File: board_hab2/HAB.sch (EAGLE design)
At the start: 39 parts, among them Q1 2N5496, Q2 2N5496, T2 2N3904

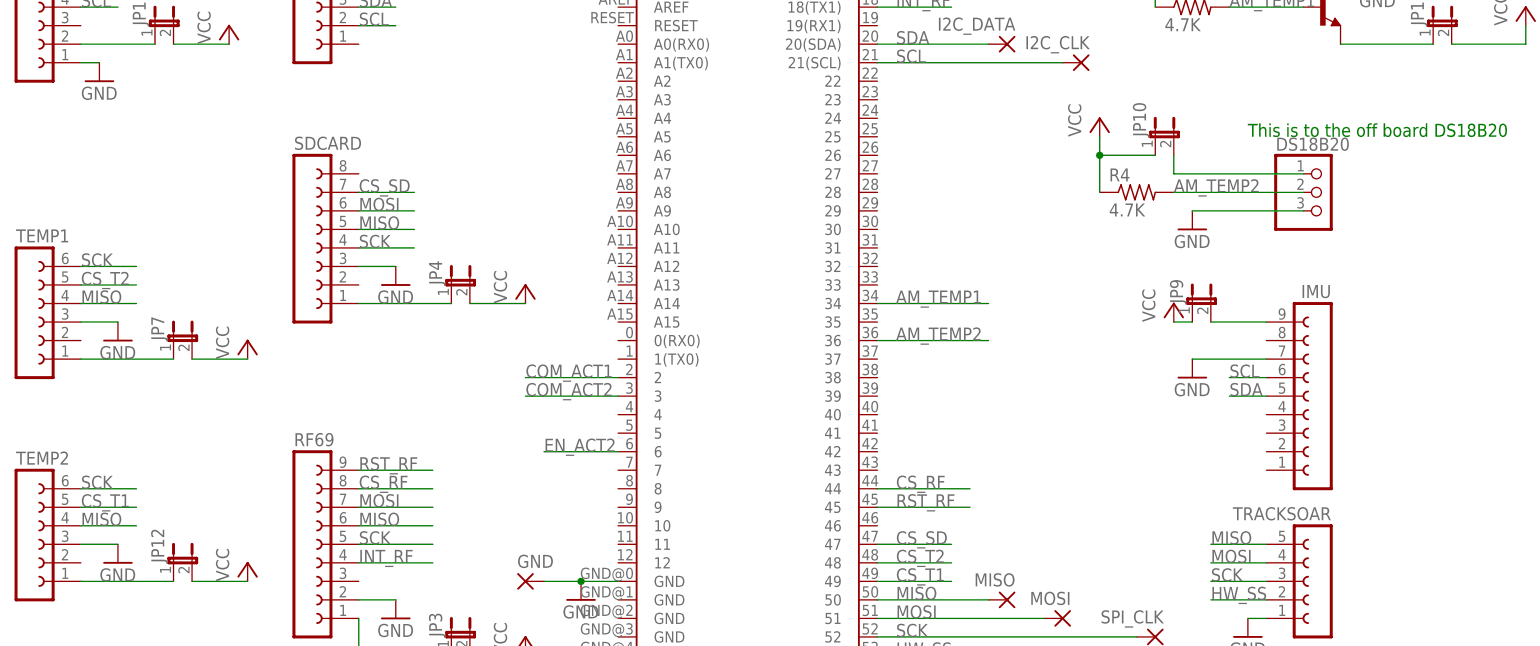
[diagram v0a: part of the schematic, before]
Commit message: Added gerbers and updated thick trace
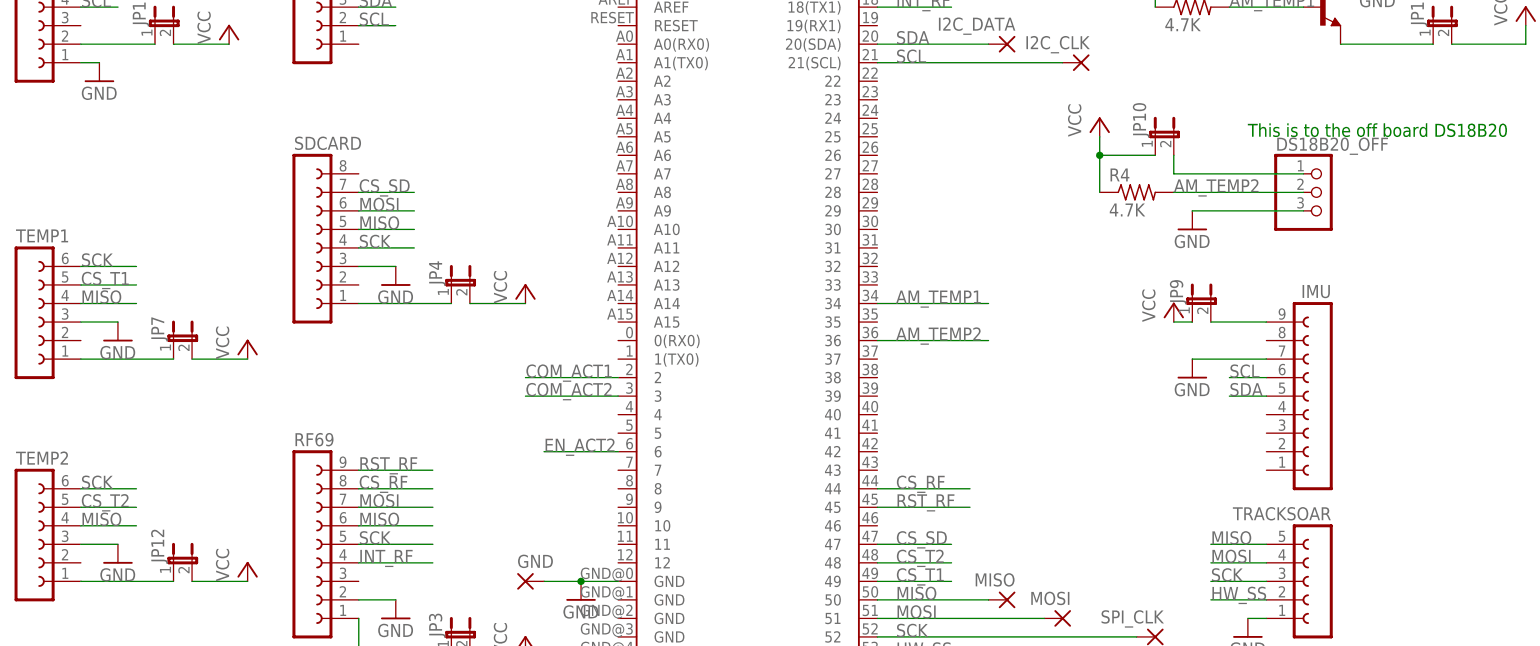
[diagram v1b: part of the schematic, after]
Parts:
- renumbered DS18B20 to DS18B20_OFF
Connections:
- net CS_T1: now also TEMP1.5; no longer TEMP2.5
- net CS_T2: now also TEMP2.5; no longer TEMP1.5
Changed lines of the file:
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@@
 <part name="JP9" library="jumper" library_urn="urn:adsk.eagle:library:252" deviceset="JP1E" device=""/>
 <part name="GND10" library="supply1" library_urn="urn:adsk.eagle:library:371" deviceset="GND" device=""/>
-<part name="DS18B20" library="adafruit" deviceset="PINHD-1X3" device=""/>
+<part name="DS18B20_OFF" library="adafruit" deviceset="PINHD-1X3" device=""/>
 <part name="JP10" library="jumper" library_urn="urn:adsk.eagle:library:252" deviceset="JP1E" device=""/>
 <part name="GND11" library="supply1" library_urn="urn:adsk.eagle:library:371" deviceset="GND" device=""/>
@@
 <instance part="JP9" gate="A" x="111.76" y="40.64"/>
 <instance part="GND10" gate="1" x="111.76" y="30.48"/>
-<instance part="DS18B20" gate="A" x="129.54" y="55.88"/>
+<instance part="DS18B20_OFF" gate="A" x="129.54" y="55.88"/>
 <instance part="JP10" gate="A" x="106.68" y="63.5"/>
 <instance part="GND11" gate="1" x="111.76" y="50.8"/>
@@
 </segment>
 <segment>
-<pinref part="DS18B20" gate="A" pin="3"/>
+<pinref part="DS18B20_OFF" gate="A" pin="3"/>
 <pinref part="GND11" gate="1" pin="GND"/>
 <wire x1="127" y1="53.34" x2="111.76" y2="53.34" width="0.1524" layer="91"/>
@@
 </segment>
 <segment>
-<pinref part="TEMP1" gate="G$1" pin="5"/>
-<wire x1="-40.64" y1="43.18" x2="-33.02" y2="43.18" width="0.1524" layer="91"/>
-<label x="-40.64" y="43.18" size="1.778" layer="95"/>
+<pinref part="TEMP2" gate="G$1" pin="5"/>
+<wire x1="-40.64" y1="12.7" x2="-33.02" y2="12.7" width="0.1524" layer="91"/>
+<label x="-40.64" y="12.7" size="1.778" layer="95"/>
 </segment>
 </net>
@@
 <segment>
 <wire x1="127" y1="55.88" x2="109.22" y2="55.88" width="0.1524" layer="91"/>
-<pinref part="DS18B20" gate="A" pin="2"/>
+<pinref part="DS18B20_OFF" gate="A" pin="2"/>
 <label x="109.22" y="55.88" size="1.778" layer="95"/>
 <pinref part="R4" gate="G$1" pin="2"/>
@@
 <segment>
 <pinref part="JP10" gate="A" pin="2"/>
-<pinref part="DS18B20" gate="A" pin="1"/>
+<pinref part="DS18B20_OFF" gate="A" pin="1"/>
 <wire x1="109.22" y1="60.96" x2="109.22" y2="58.42" width="0.1524" layer="91"/>
 <wire x1="109.22" y1="58.42" x2="127" y2="58.42" width="0.1524" layer="91"/>
@@
 </segment>
 <segment>
-<pinref part="TEMP2" gate="G$1" pin="5"/>
-<wire x1="-40.64" y1="12.7" x2="-33.02" y2="12.7" width="0.1524" layer="91"/>
-<label x="-40.64" y="12.7" size="1.778" layer="95"/>
-</segment>
-</net>
+<pinref part="TEMP1" gate="G$1" pin="5"/>
+<wire x1="-40.64" y1="43.18" x2="-33.02" y2="43.18" width="0.1524" layer="91"/>
+<label x="-40.64" y="43.18" size="1.778" layer="95"/>
+</segment>
+</net>
